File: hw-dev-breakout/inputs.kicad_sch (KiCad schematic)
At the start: 87 parts, among them J201 WAGO 250-216, J202 Conn_01x16, U201 CM1293A-04SO, U202 CM1293A-04SO, U203 CM1293A-04SO, U204 CM1293A-04SO, U205 CM1293A-04SO

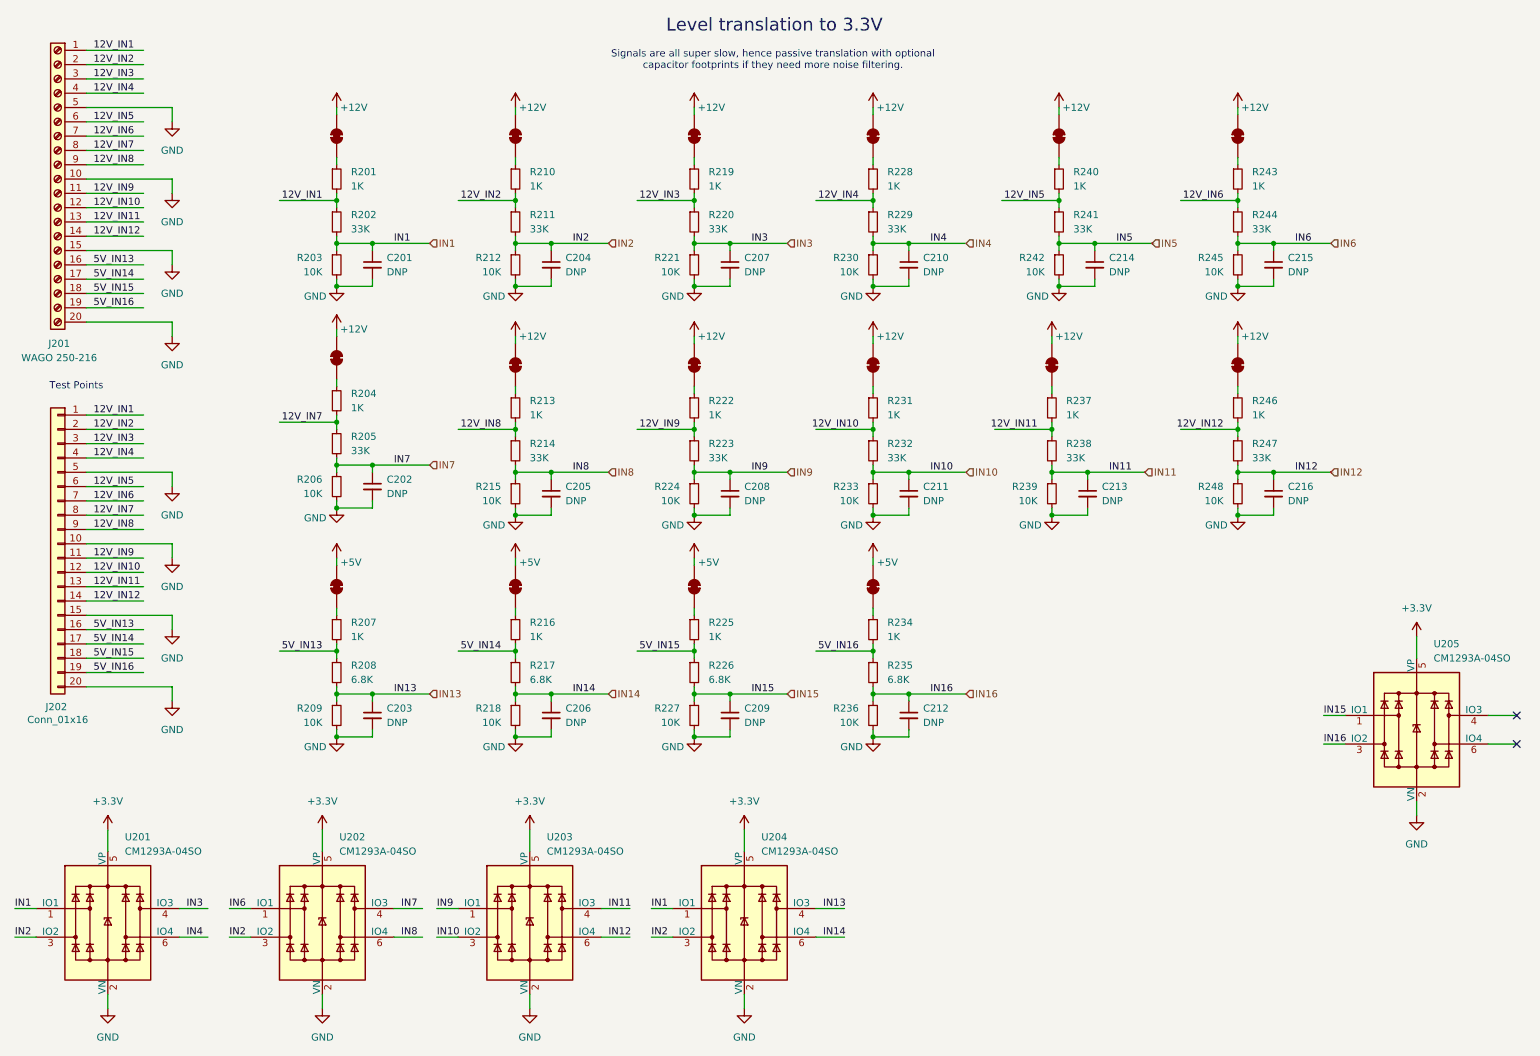
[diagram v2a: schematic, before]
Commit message: pcb: Initial components placed
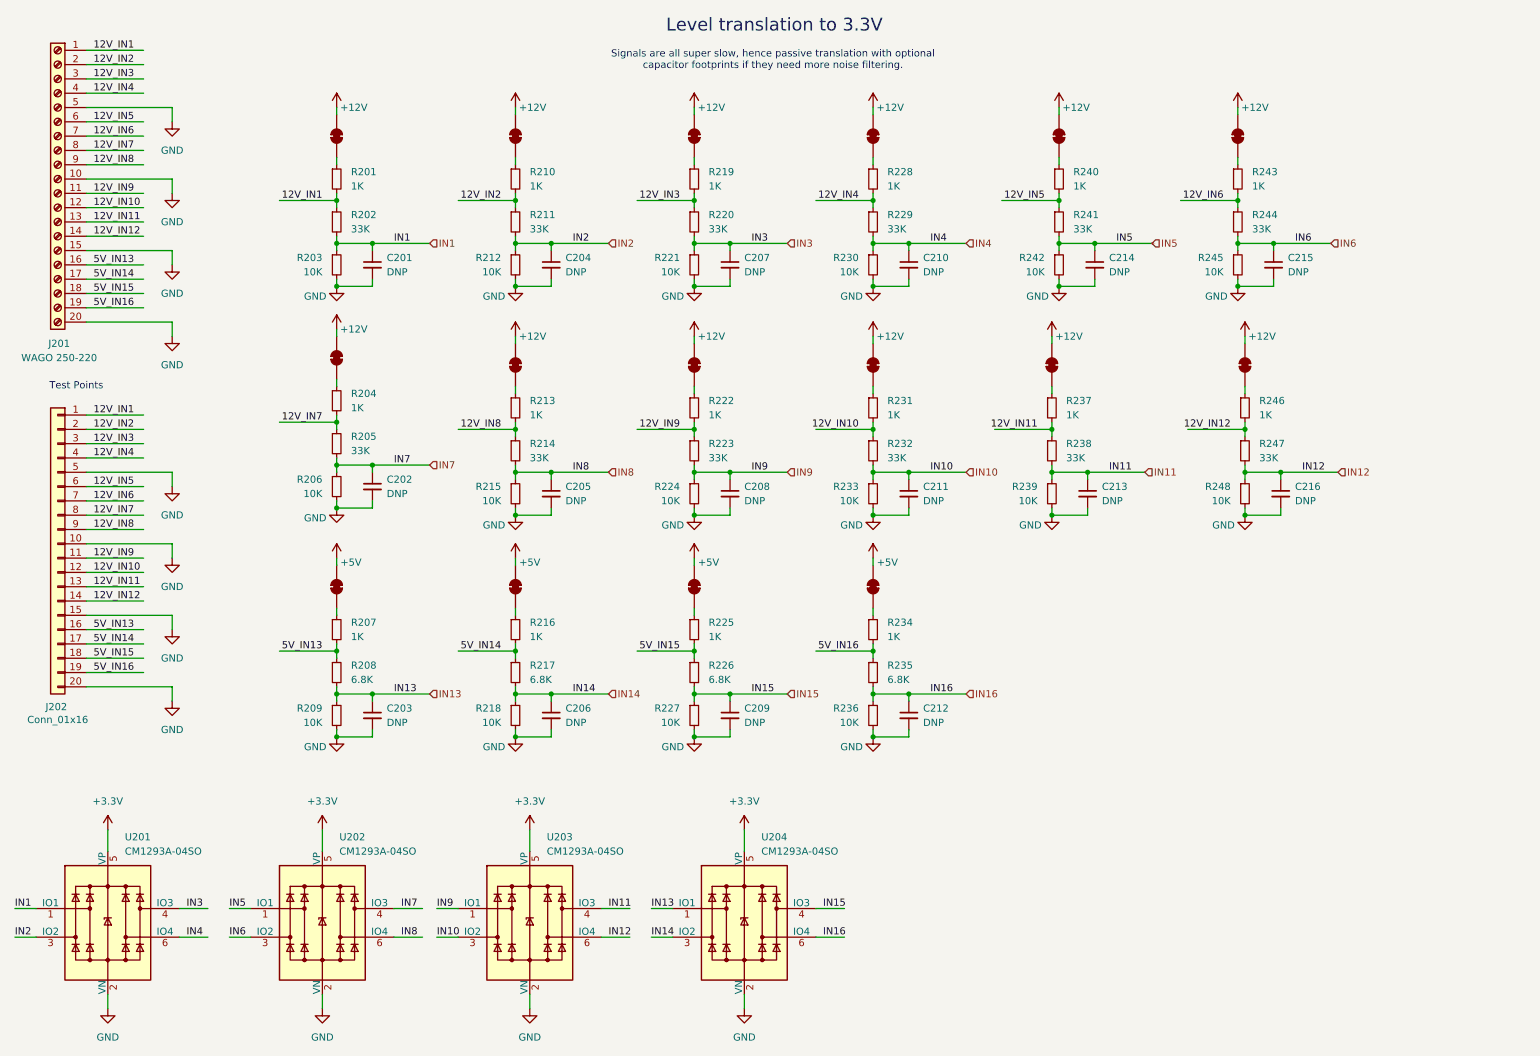
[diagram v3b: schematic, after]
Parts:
- removed U205: CM1293A-04SO, Package_TO_SOT_SMD:SOT-23-6, symbol Power_Protection:CDSOT236-0504C
- J201: value WAGO 250-216 -> WAGO 250-220
- J202: footprint Connector_PinHeader_2.54mm:PinHeader_1x01_P2.54mm_Vertical -> Connector_PinSocket_2.54mm:PinSocket_1x20_P2.54mm_Vertical
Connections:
- net IN1: no longer U204.1 (IO1)
- net IN12: no longer C214.1, R241.2, R242.1
- net IN13: now also U204.1 (IO1); no longer U204.4 (IO3)
- net IN14: now also U204.3 (IO2); no longer U204.6 (IO4)
- net IN15: now also U204.4 (IO3)
- net IN16: now also U204.6 (IO4)
- net IN2: no longer U202.3 (IO2), U204.3 (IO2)
- net IN6: now also U202.3 (IO2); no longer U202.1 (IO1)
- new net IN5: C214.1, R241.2, R242.1, U202.1 (IO1)
- no-connect marks 2 -> 0

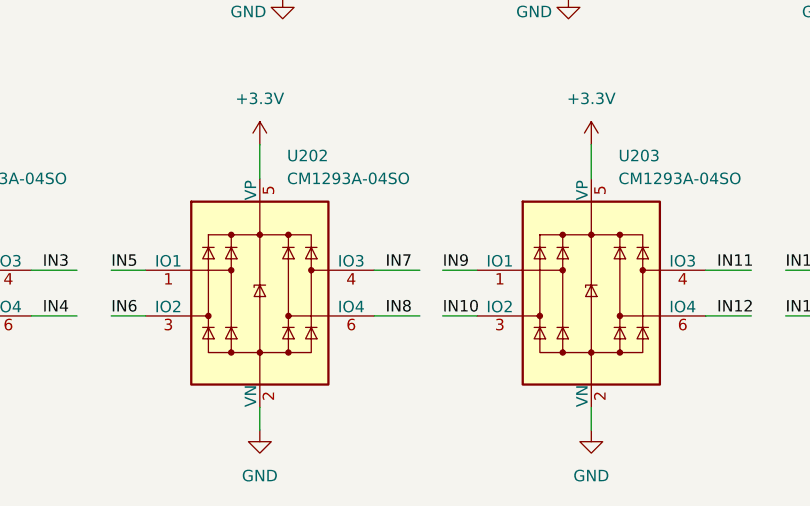
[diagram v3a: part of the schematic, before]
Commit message: pcb: Partially routed
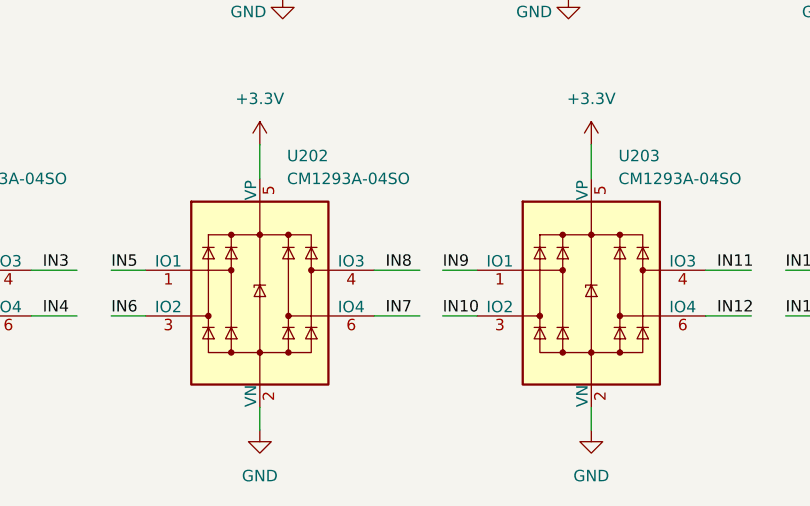
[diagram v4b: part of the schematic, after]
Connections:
- net IN7: now also U202.6 (IO4); no longer U202.4 (IO3)
- net IN8: now also U202.4 (IO3); no longer U202.6 (IO4)
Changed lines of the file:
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@@
 	)
 	(label "IN8"
-		(at 82.55 177.8 0)
+		(at 82.55 172.72 0)
 		(fields_autoplaced yes)
 		(effects
@@
 	)
 	(label "IN7"
-		(at 82.55 172.72 0)
-		(fields_autoplaced yes)
-		(effects
+		(at 82.55 177.8 0)
+		(fields_autoplaced yes)
+		(effects

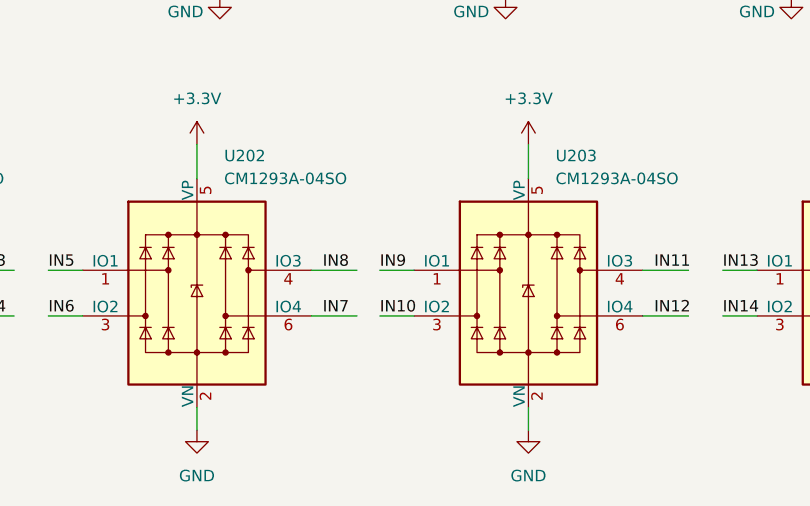
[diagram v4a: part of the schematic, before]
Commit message: pcb: Routed, using jlc 4 layer specs
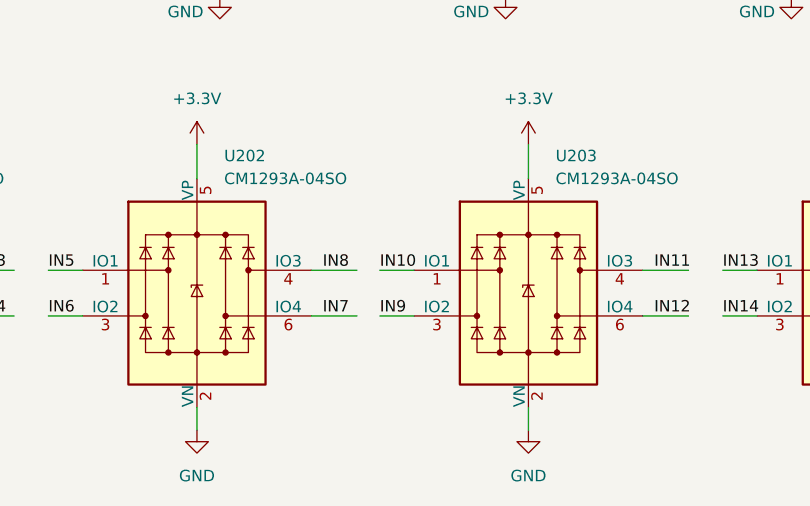
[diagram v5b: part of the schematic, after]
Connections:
- net IN10: now also U203.1 (IO1); no longer U203.3 (IO2)
- net IN9: now also U203.3 (IO2); no longer U203.1 (IO1)
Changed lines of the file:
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@@
 	)
 	(label "IN9"
-		(at 88.9 172.72 0)
+		(at 88.9 177.8 0)
 		(fields_autoplaced yes)
 		(effects
@@
 	)
 	(label "IN10"
-		(at 88.9 177.8 0)
-		(fields_autoplaced yes)
-		(effects
+		(at 88.9 172.72 0)
+		(fields_autoplaced yes)
+		(effects

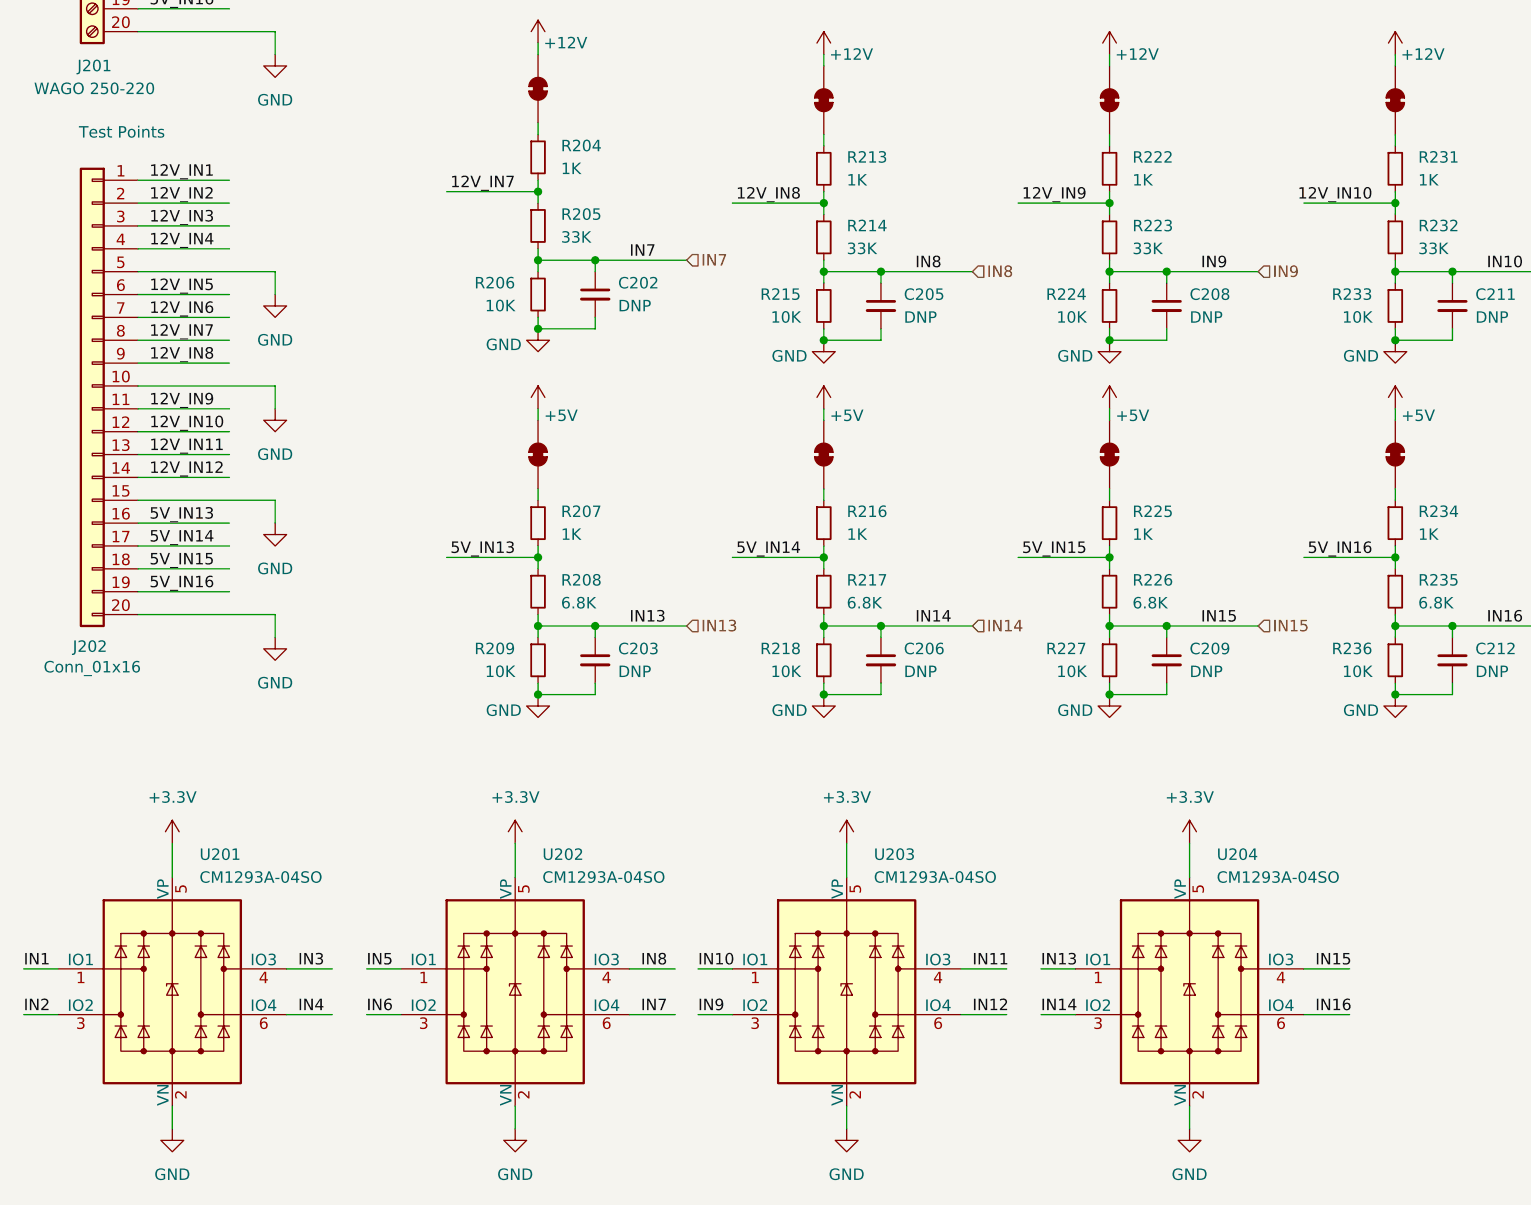
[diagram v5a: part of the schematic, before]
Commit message: pcb: Routed for 2 layer, fixed P-fet error
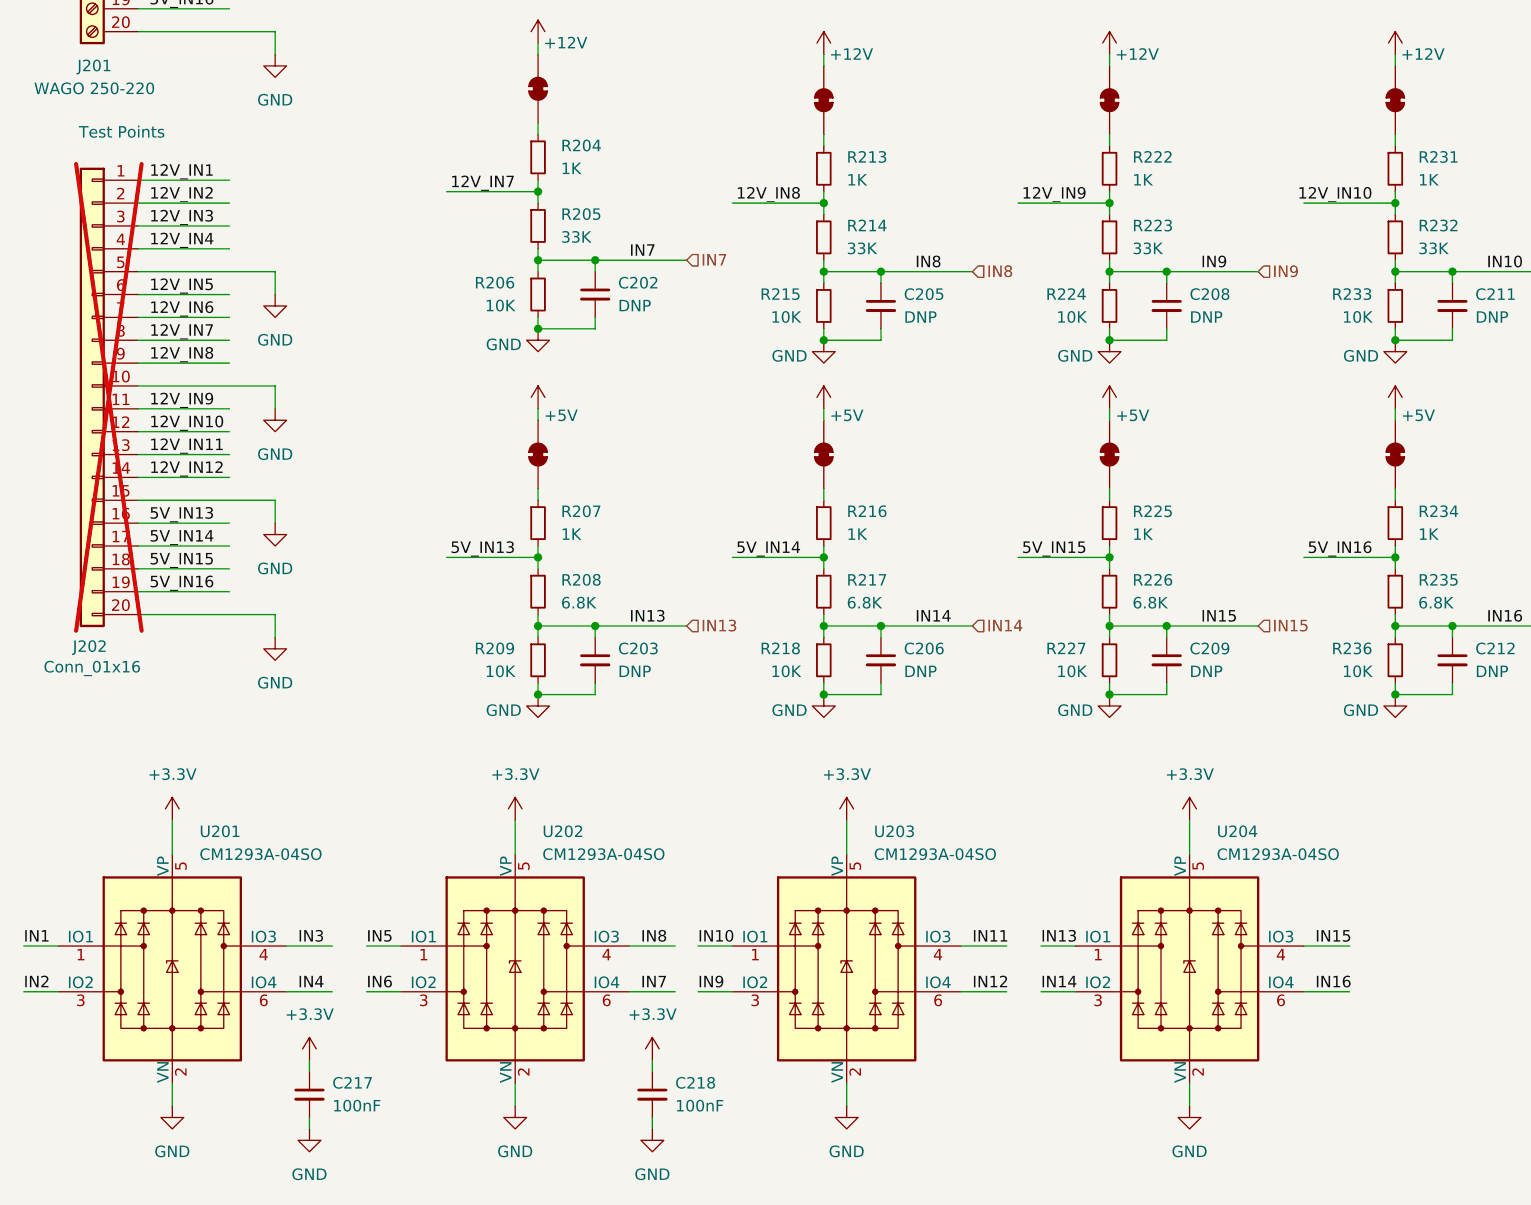
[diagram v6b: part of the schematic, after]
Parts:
- added C217, C218: 100nF, Capacitor_SMD:C_0603_1608Metric, symbol Device:C_Small
- J201: footprint hw-dev-breakout:CONN-TH_250-220 -> hw-dev-breakout:WAGO 250-22
- J202: now not fitted
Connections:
- net +3.3V: now also C217.1, C218.1
- net GND: now also C217.2, C218.2
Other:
- moved on the sheet: U201, U202, U203, U204

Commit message: Final cleanups for initial fab run
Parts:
- C201, C202, C203, C204, C205, C206, C207, C208, C209, C210, C211, C212, C213, C214, C215, C216, JP201, JP202, JP203, JP204, JP205, JP206, JP207, JP208, JP209, JP210, JP211, JP212, JP213, JP214, JP215, JP216: now not fitted
- C217, C218: LCSC Part # (none) -> C14663
- J201: LCSC Part # (none) -> C2833599
- R201, R204, R207, R210, R213, R216, R219, R222, R225, R228, R231, R234, R237, R240, R243, R246: LCSC Part # (none) -> C21190
- R202, R205, R211, R214, R220, R223, R229, R232, R238, R241, R244, R247: LCSC Part # (none) -> C4216
- R203, R206, R209, R212, R215, R218, R221, R224, R227, R230, R233, R236, R239, R242, R245, R248: LCSC Part # (none) -> C25804
- R208, R217, R226, R235: LCSC Part # (none) -> C23212
- U201, U202, U203, U204: LCSC Part # (none) -> C393377
